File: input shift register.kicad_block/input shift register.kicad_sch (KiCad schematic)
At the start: 10 parts, among them U3 74HC165

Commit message: adjusted footprint sizes (THT) and label naming for input shifter.
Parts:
- removed R19, R20, R21, R22, R23, R24: 10k, Resistor_THT:R_Axial_DIN0309_L9.0mm_D3.2mm_P12.70mm_Horizontal, symbol Device:R
- removed U3: 74HC165, Package_DIP:DIP-16_W7.62mm_Socket_LongPads, symbol 74xx:74HC165
- added R2, R3, R4, R5, R6, R7: 10k, Resistor_THT:R_Axial_DIN0207_L6.3mm_D2.5mm_P10.16mm_Horizontal, symbol Device:R
- added U1: 74HC165, Package_DIP:DIP-16_W7.62mm_Socket_LongPads, symbol 74xx:74HC165
- R27: renamed from R26; footprint Resistor_THT:R_Axial_DIN0309_L9.0mm_D3.2mm_P12.70mm_Horizontal -> Resistor_THT:R_Axial_DIN0207_L6.3mm_D2.5mm_P10.16mm_Horizontal
- R8: renamed from R25; footprint Resistor_THT:R_Axial_DIN0309_L9.0mm_D3.2mm_P12.70mm_Horizontal -> Resistor_THT:R_Axial_DIN0207_L6.3mm_D2.5mm_P10.16mm_Horizontal
- renumbered C4 to C1
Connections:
- net GND: now also U1.10 (DS), U1.15 (~{CE}), U1.8 (GND)
- net VCC: now also R2.1, R3.1, R4.1, R5.1, R6.1, R7.1, U1.16 (VCC)
- net IS_SWITCH7 renamed IS SWITCH 7
- net IS SWITCH 7: now also U1.5 (D6)
- net IS_SWITCH8 renamed IS SWITCH 8
- net IS SWITCH 8: now also U1.6 (D7)
- new net IS CLOCK: U1.2 (CP)
- new net IS DATA: U1.9 (Q7)
- new net IS LATCH: U1.1 (~{PL})
- new net IS SWITCH 1: R2.2, U1.11 (D0)
- new net IS SWITCH 2: R3.2, U1.12 (D1)
- new net IS SWITCH 3: R4.2, U1.13 (D2)
- new net IS SWITCH 4: R5.2, U1.14 (D3)
- new net IS SWITCH 5: R6.2, U1.3 (D4)
- new net IS SWITCH 6: R7.2, U1.4 (D5)
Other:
- moved on the sheet: C1

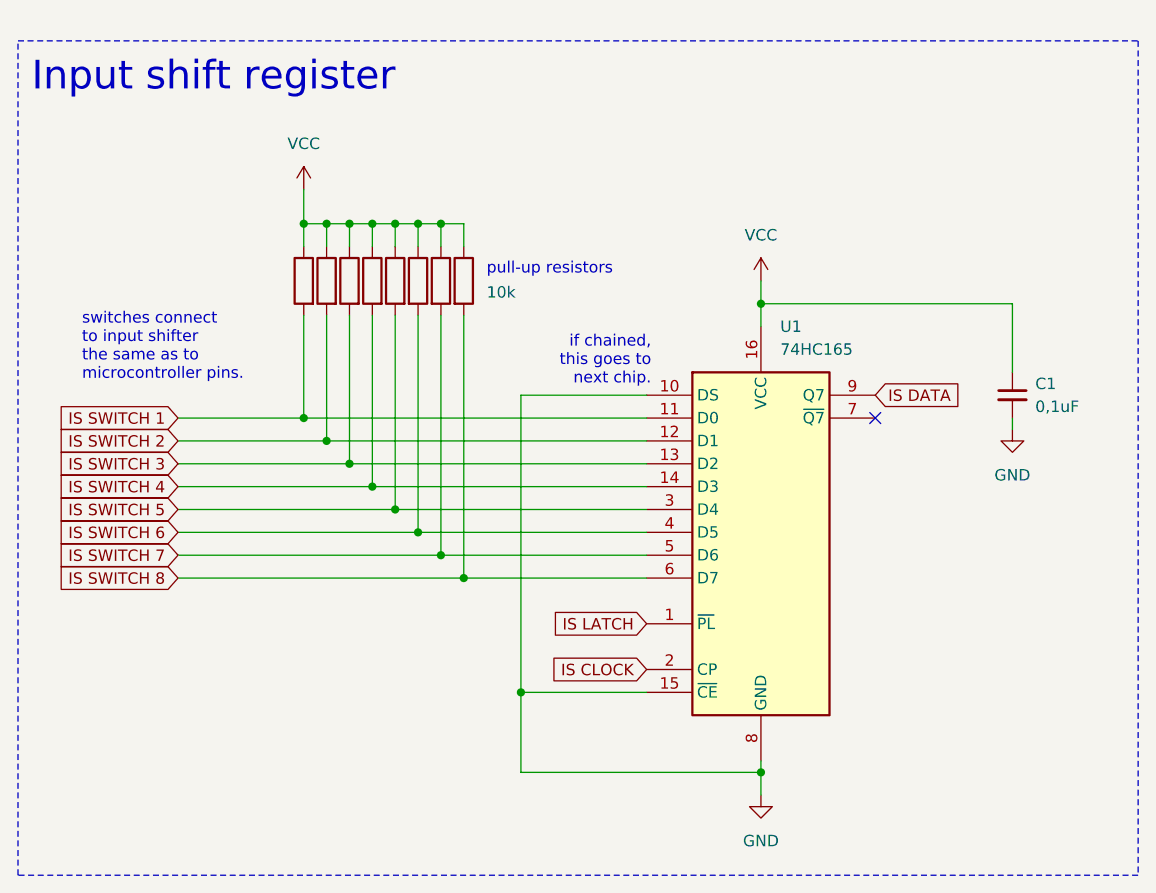
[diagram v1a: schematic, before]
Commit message: added daisy chain info
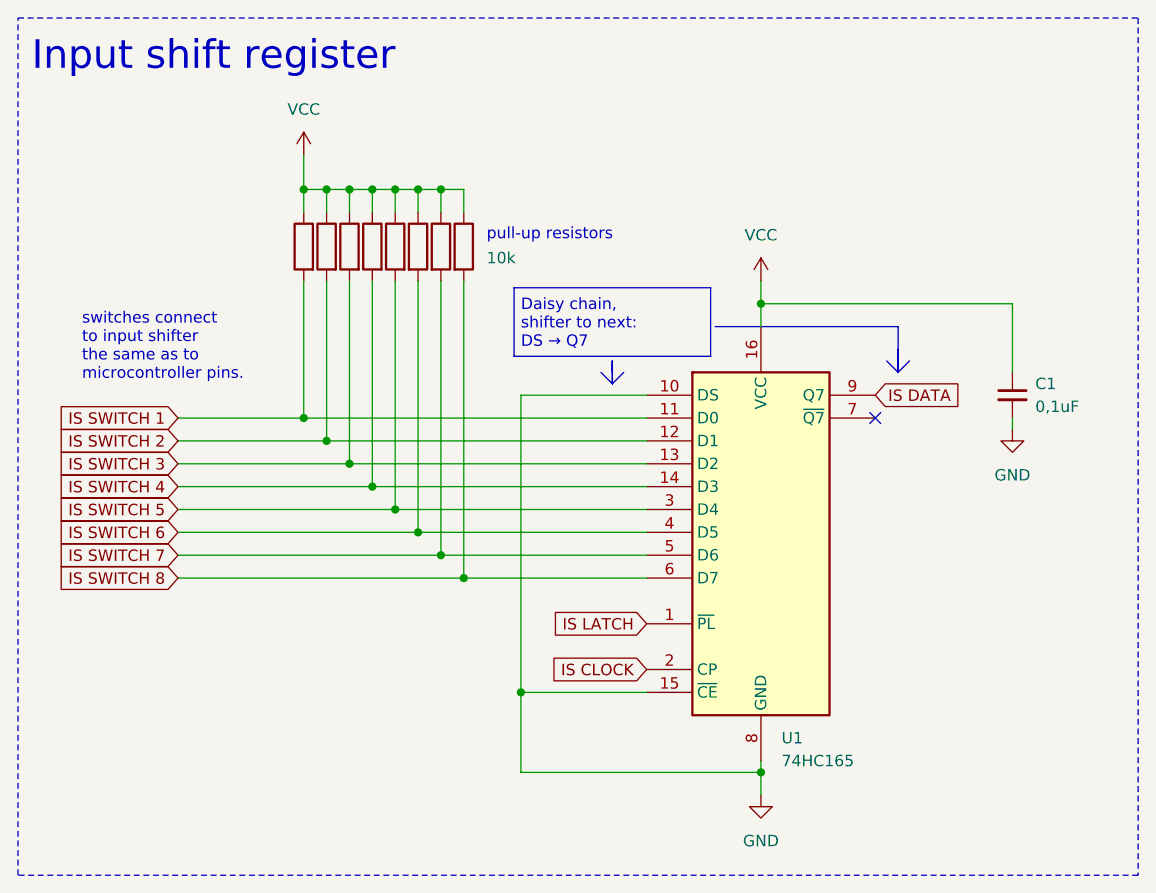
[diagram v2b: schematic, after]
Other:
- note added: "Daisy chain, shifter to next: DS → Q7"
- note removed: "if chained, this goes to next chip."
